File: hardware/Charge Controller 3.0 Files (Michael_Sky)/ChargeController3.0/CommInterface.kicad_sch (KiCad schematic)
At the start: 16 parts, among them J13 Conn-1x2, J14 Conn-1x2, J15 Conn-1x2, J17 SCL_MAS_01x01_Pin, J18 SDA_MAS_01x01_Pin, J4 3.3V_PULLUP_01x02_Pin

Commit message: New formatting
New formatting
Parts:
- removed J13, J14, J15: Conn-1x2, Connector_PinHeader_2.54mm:PinHeader_1x02_P2.54mm_Vertical, symbol Connector:Conn_01x02_Pin
- removed R18: 10k, Resistor_SMD:R_0603_1608Metric, symbol Device:R
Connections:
- net INT: now also R20.1
- net STAT_1: now also D2.1 (K)
- net 3.3V: now reaches J4.1 (Pin_1), R16.2, R17.2, R19.2, R20.2, R21.2, R22.2
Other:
- moved on the sheet: D1, D2, D3, R19, R20, R21, R22

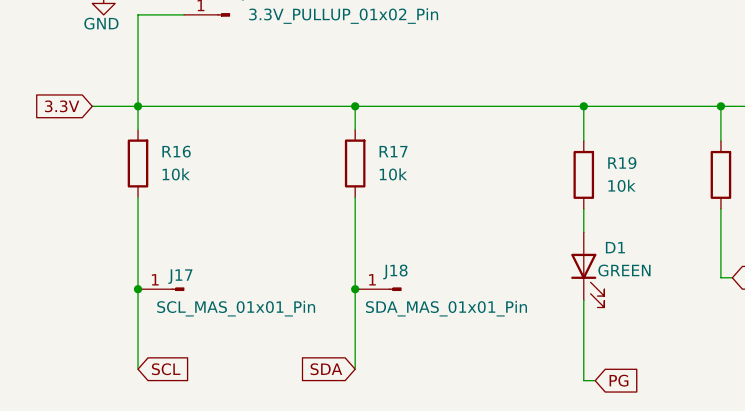
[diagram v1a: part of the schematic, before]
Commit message: Final PCB?
inhibits rework, filtering rework
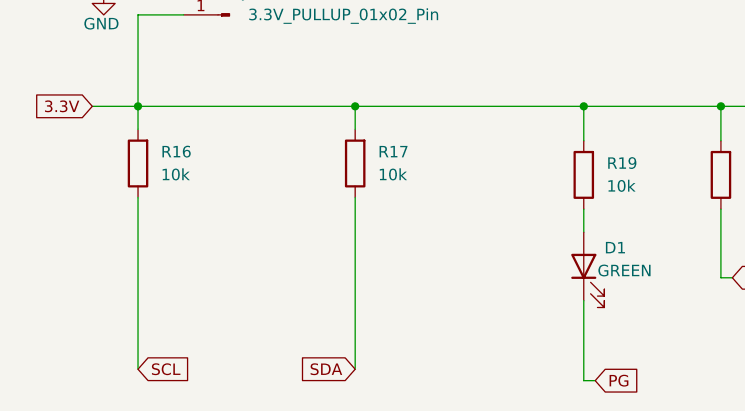
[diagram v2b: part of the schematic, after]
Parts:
- removed J17: SCL_MAS_01x01_Pin, Connector_PinHeader_2.54mm:PinHeader_1x01_P2.54mm_Vertical, symbol Connector:Conn_01x01_Pin
- removed J18: SDA_MAS_01x01_Pin, Connector_PinHeader_2.54mm:PinHeader_1x01_P2.54mm_Vertical, symbol Connector:Conn_01x01_Pin
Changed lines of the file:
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@@
-	)
-	(junction
-		(at 107.95 102.87)
-		(diameter 0)
-		(color 0 0 0 0)
-	)
-	(junction
-		(at 83.82 102.87)
-		(diameter 0)
-		(color 0 0 0 0)
 	)
 	(junction
@@
 	(wire
 		(pts
-			(xy 107.95 102.87) (xy 107.95 111.76)
+			(xy 107.95 92.71) (xy 107.95 111.76)
 		)
 		(stroke
@@
 	(wire
 		(pts
-			(xy 83.82 92.71) (xy 83.82 102.87)
+			(xy 83.82 92.71) (xy 83.82 111.76)
 		)
 		(stroke
@@
 	(wire
 		(pts
-			(xy 83.82 102.87) (xy 83.82 111.76)
-		)
-		(stroke
-			(width 0)
-			(type default)
-		)
-	)
-	(wire
-		(pts
 			(xy 148.59 93.98) (xy 148.59 101.6)
 		)
@@
 		(pts
 			(xy 182.88 109.22) (xy 181.61 109.22)
-		)
-		(stroke
-			(width 0)
-			(type default)
-		)
-	)
-	(wire
-		(pts
-			(xy 107.95 92.71) (xy 107.95 102.87)
 		)
 		(stroke
@@
 	)
 	(symbol
-		(lib_id "Connector:Conn_01x01_Pin")
-		(at 113.03 102.87 180)
-		(unit 1)
-		(body_style 1)
-		(exclude_from_sim no)
-		(in_bom yes)
-		(on_board yes)
-		(in_pos_files yes)
-		(dnp no)
-		(property "Reference" "J18"
-			(at 112.522 100.838 0)
-			(show_name no)
-			(do_not_autoplace no)
-			(effects
-				(font
-					(size 1.27 1.27)
-				)
-			)
-		)
-		(property "Value" "SDA_MAS_01x01_Pin"
-			(at 118.11 104.902 0)
-			(show_name no)
-			(do_not_autoplace no)
-			(effects
-				(font
-					(size 1.27 1.27)
-				)
-			)
-		)
-		(property "Footprint" "Connector_PinHeader_2.54mm:PinHeader_1x01_P2.54mm_Vertical"
-			(at 113.03 102.87 0)
-			(hide yes)
-			(show_name no)
-			(do_not_autoplace no)
-			(effects
-				(font
-					(size 1.27 1.27)
-				)
-			)
-		)
-		(property "Datasheet" ""
-			(at 113.03 102.87 0)
-			(hide yes)
-			(show_name no)
-			(do_not_autoplace no)
-			(effects
-				(font
-					(size 1.27 1.27)
-				)
-			)
-		)
-		(property "Description" "Generic connector, single row, 01x01, script generated"
-			(at 113.03 102.87 0)
-			(hide yes)
-			(show_name no)
-			(do_not_autoplace no)
-			(effects
-				(font
-					(size 1.27 1.27)
-				)
-			)
-		)
-		(pin "1"
-		)
-		(instances
-			(project "ChargeController3.0"
-				(path "/a54826c2-d365-4450-b7a8-71945dba02c0/8779625f-bbe1-4b47-be0c-e79d9164e4be"
-					(reference "J18")
-					(unit 1)
-				)
-			)
-		)
-	)
-	(symbol
 		(lib_id "Connector:Conn_01x02_Pin")
 		(at 93.98 72.39 180)
@@
 					(unit 1)
 				)
-			)
-		)
-	)
-	(symbol
-		(lib_id "Connector:Conn_01x01_Pin")
-		(at 88.9 102.87 180)
-		(unit 1)
-		(body_style 1)
-		(exclude_from_sim no)
-		(in_bom yes)
-		(on_board yes)
-		(in_pos_files yes)
-		(dnp no)
-		(property "Reference" "J17"
-			(at 88.646 101.346 0)
-			(show_name no)
-			(do_not_autoplace no)
-			(effects
-				(font
-					(size 1.27 1.27)
-				)
-			)
-		)
-		(property "Value" "SCL_MAS_01x01_Pin"
-			(at 94.742 104.902 0)
-			(show_name no)
-			(do_not_autoplace no)
-			(effects
-				(font
-					(size 1.27 1.27)
-				)
-			)
-		)
-		(property "Footprint" "Connector_PinHeader_2.54mm:PinHeader_1x01_P2.54mm_Vertical"
-			(at 88.9 102.87 0)
-			(hide yes)
-			(show_name no)
-			(do_not_autoplace no)
-			(effects
-				(font
-					(size 1.27 1.27)
-				)
-			)
-		)
-		(property "Datasheet" ""
-			(at 88.9 102.87 0)
-			(hide yes)
-			(show_name no)
-			(do_not_autoplace no)
-			(effects
-				(font
-					(size 1.27 1.27)
-				)
-			)
-		)
-		(property "Description" "Generic connector, single row, 01x01, script generated"
-			(at 88.9 102.87 0)
-			(hide yes)
-			(show_name no)
-			(do_not_autoplace no)
-			(effects
-				(font
-					(size 1.27 1.27)
-				)
-			)
-		)
-		(pin "1"
-		)
-		(instances
-			(project "ChargeController3.0"
-				(path "/a54826c2-d365-4450-b7a8-71945dba02c0/8779625f-bbe1-4b47-be0c-e79d9164e4be"
-					(reference "J17")
-					(unit 1)
-				)
